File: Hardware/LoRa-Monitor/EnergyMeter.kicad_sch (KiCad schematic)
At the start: 76 parts, among them U14 ATM90E32AS-AU-R, U16 ADuM1401xRW, U17 ADuM1401xRW, U18 ADuM1401xRW, X1 16.384MHz

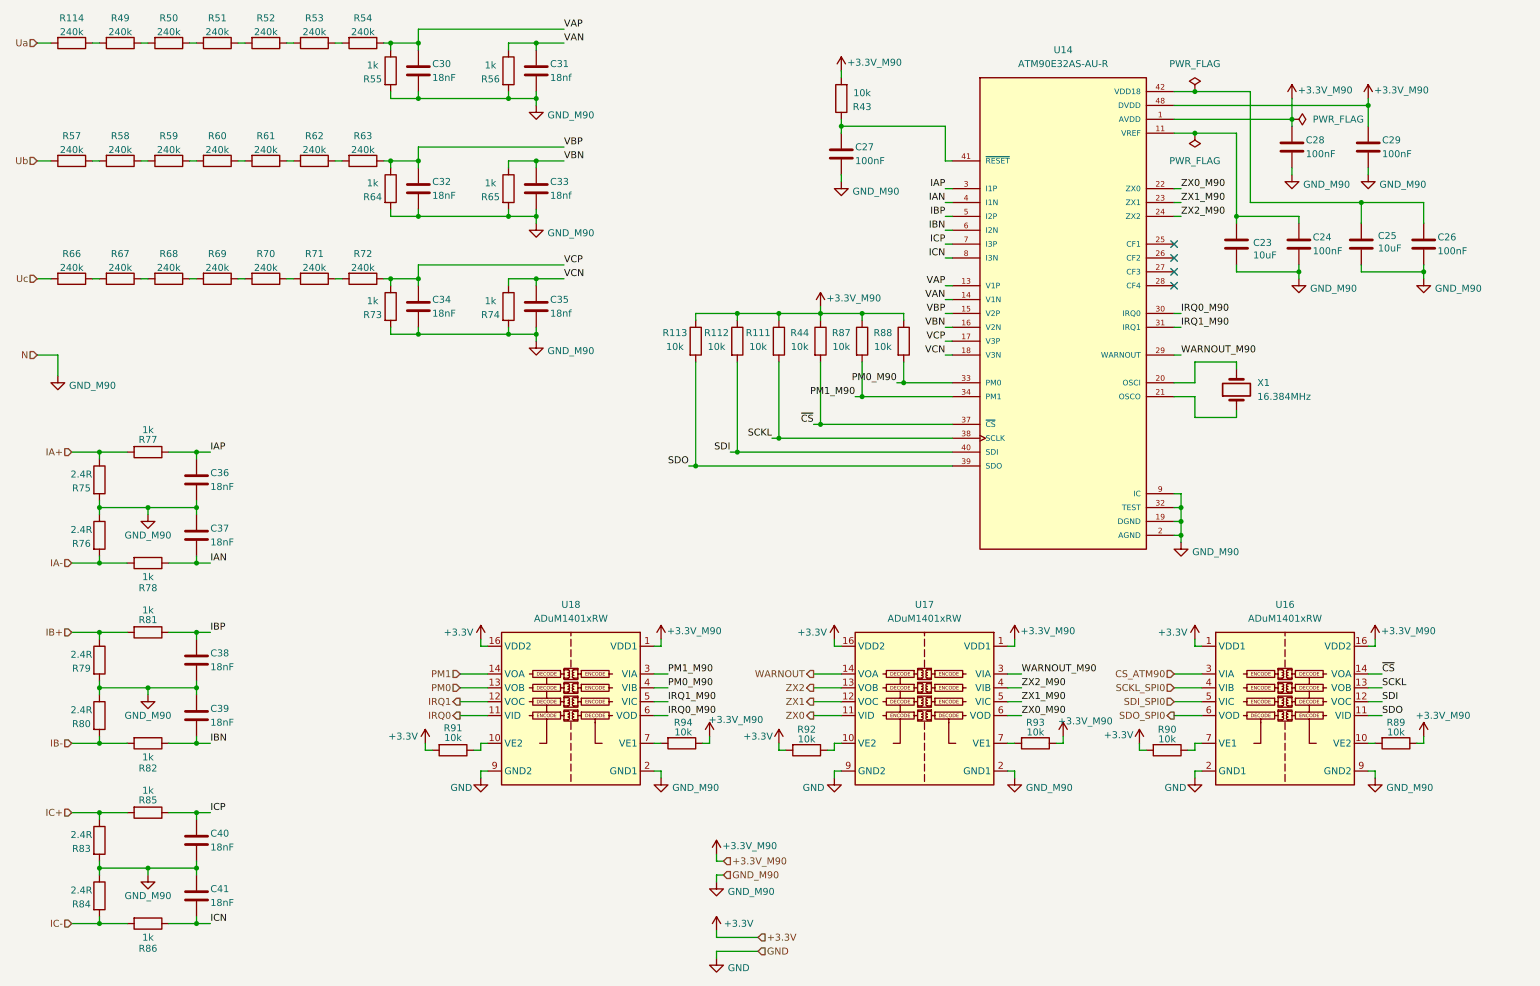
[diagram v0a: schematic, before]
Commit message: Fixed schematics and started layout
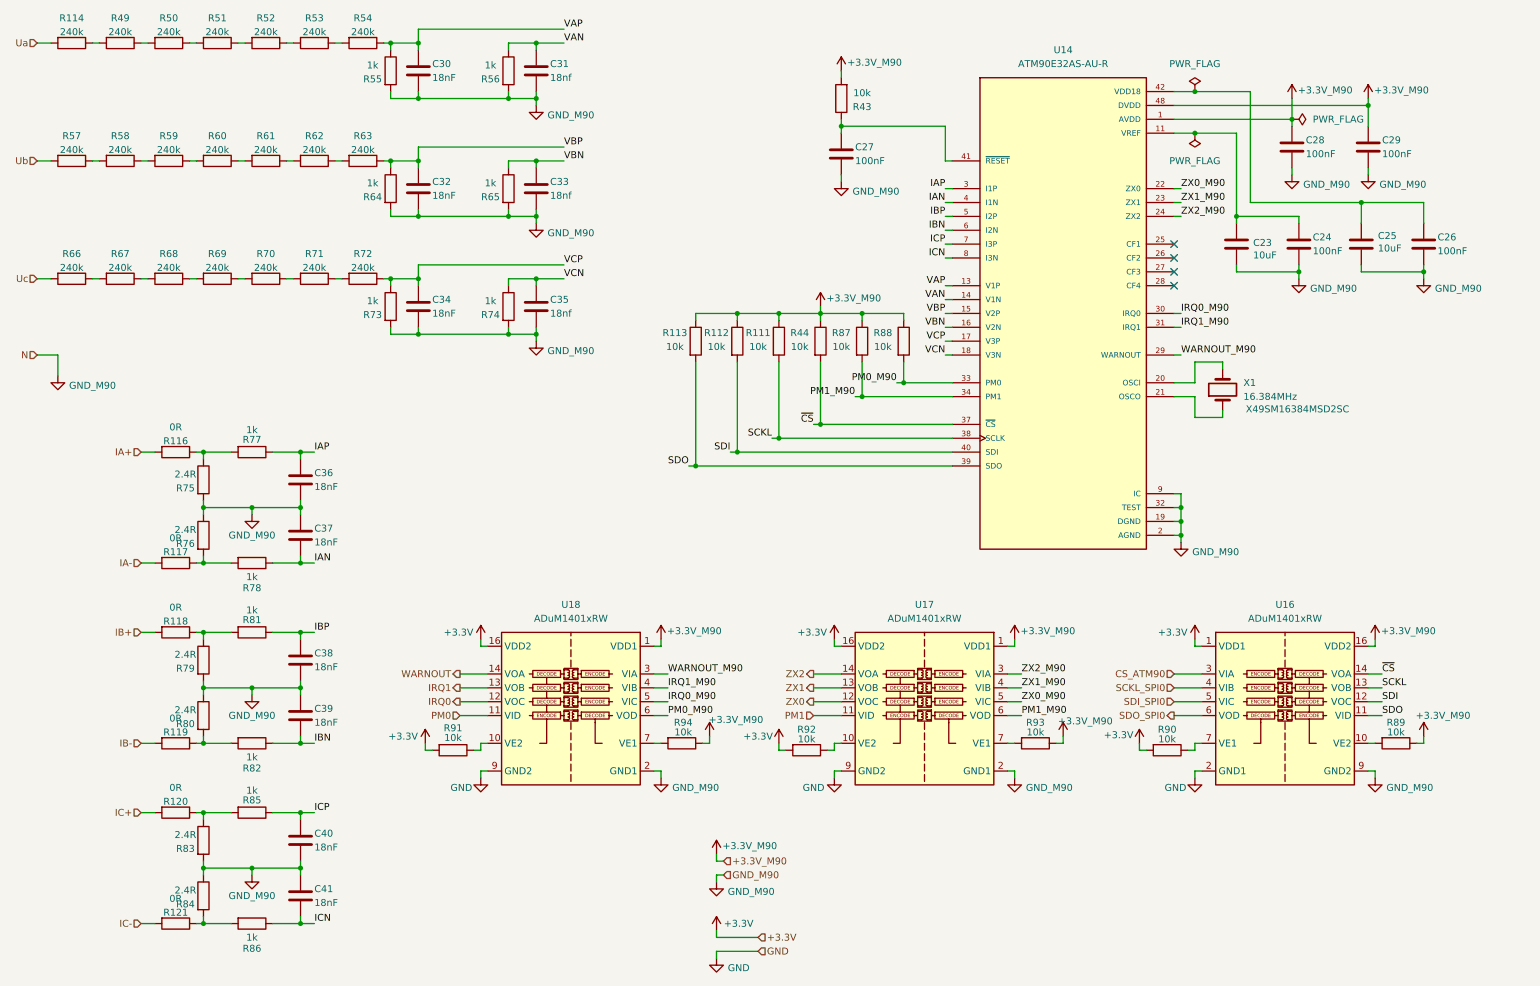
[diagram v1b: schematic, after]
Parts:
- added R116, R117, R118, R119, R120, R121: 0R, Resistor_SMD:R_0805_2012Metric, symbol Device:R
- X1: footprint (none) -> Crystal:Crystal_SMD_HC49-SD; Part # (none) -> X49SM16384MSD2SC
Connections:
- net IA+: now also R116.2; no longer R75.1, R77.2
- net IA-: now also R117.2; no longer R76.2, R78.2
- net IB+: now also R118.2; no longer R79.1, R81.2
- net IB-: now also R119.2; no longer R80.2, R82.2
- net IC+: now also R120.2; no longer R83.1, R85.2
- net IC-: now also R121.2; no longer R84.2, R86.2
- net IRQ0: now also U18.12 (VOC); no longer U18.11 (VID)
- net IRQ0_M90: now also U18.5 (VIC); no longer U18.6 (VOD)
- net IRQ1: now also U18.13 (VOB); no longer U18.12 (VOC)
- net IRQ1_M90: now also U18.4 (VIB); no longer U18.5 (VIC)
- net PM0: now also U18.11 (VID); no longer U18.13 (VOB)
- net PM0_M90: now also U18.6 (VOD); no longer U18.4 (VIB)
- net PM1: now also U17.11 (VID); no longer U18.14 (VOA)
- net PM1_M90: now also U17.6 (VOD); no longer U18.3 (VIA)
- net WARNOUT: now also U18.14 (VOA); no longer U17.14 (VOA)
- net WARNOUT_M90: now also U18.3 (VIA); no longer U17.3 (VIA)
- net ZX0: now also U17.12 (VOC); no longer U17.11 (VID)
- net ZX0_M90: now also U17.5 (VIC); no longer U17.6 (VOD)
- net ZX1: now also U17.13 (VOB); no longer U17.12 (VOC)
- net ZX1_M90: now also U17.4 (VIB); no longer U17.5 (VIC)
- net ZX2: now also U17.14 (VOA); no longer U17.13 (VOB)
- net ZX2_M90: now also U17.3 (VIA); no longer U17.4 (VIB)
- new net: R116.1, R75.1, R77.2
- new net: R117.1, R76.2, R78.2
- new net: R121.1, R84.2, R86.2
- new net: R120.1, R83.1, R85.2
- new net: R118.1, R79.1, R81.2
- new net: R119.1, R80.2, R82.2
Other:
- moved on the sheet: C36, C37, C38, C39, C40, C41, R75, R76, R77, R78, R79, R80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

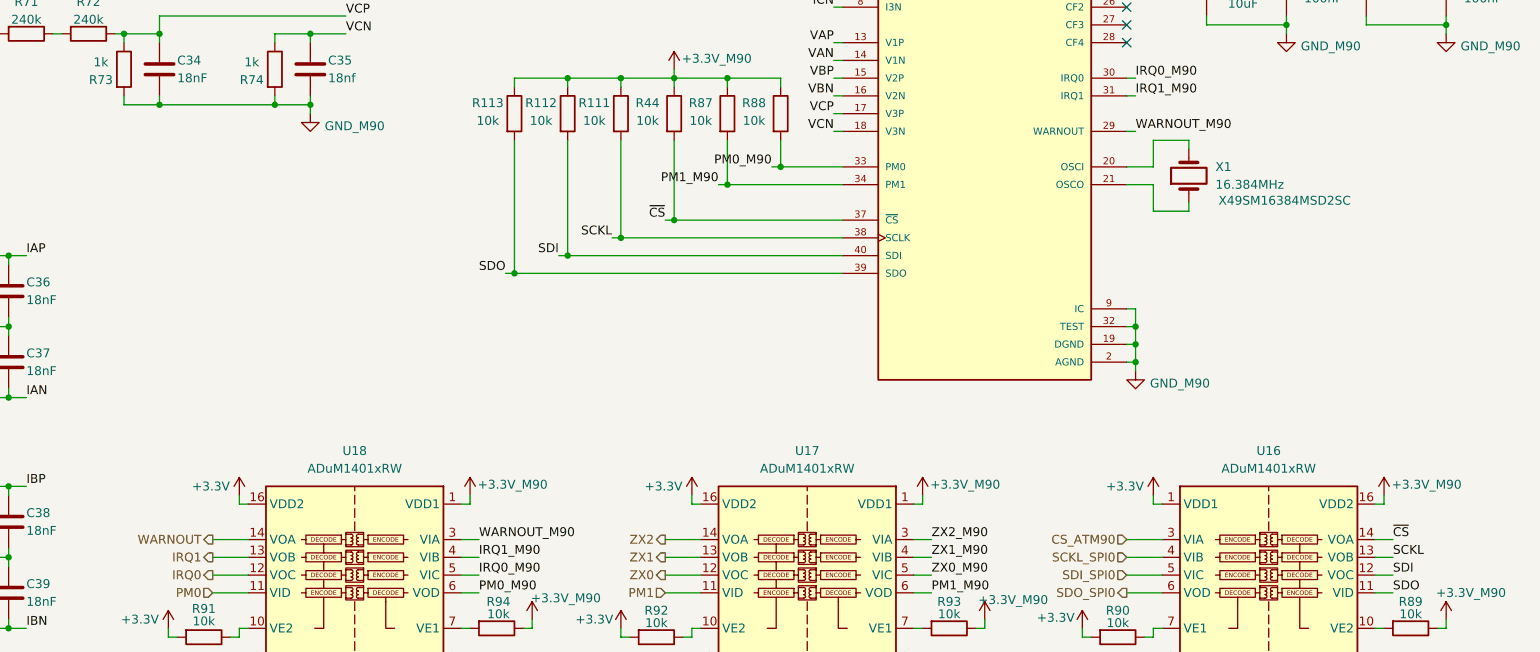
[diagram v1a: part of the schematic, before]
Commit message: Finished routing and DRC gives 0 errors.
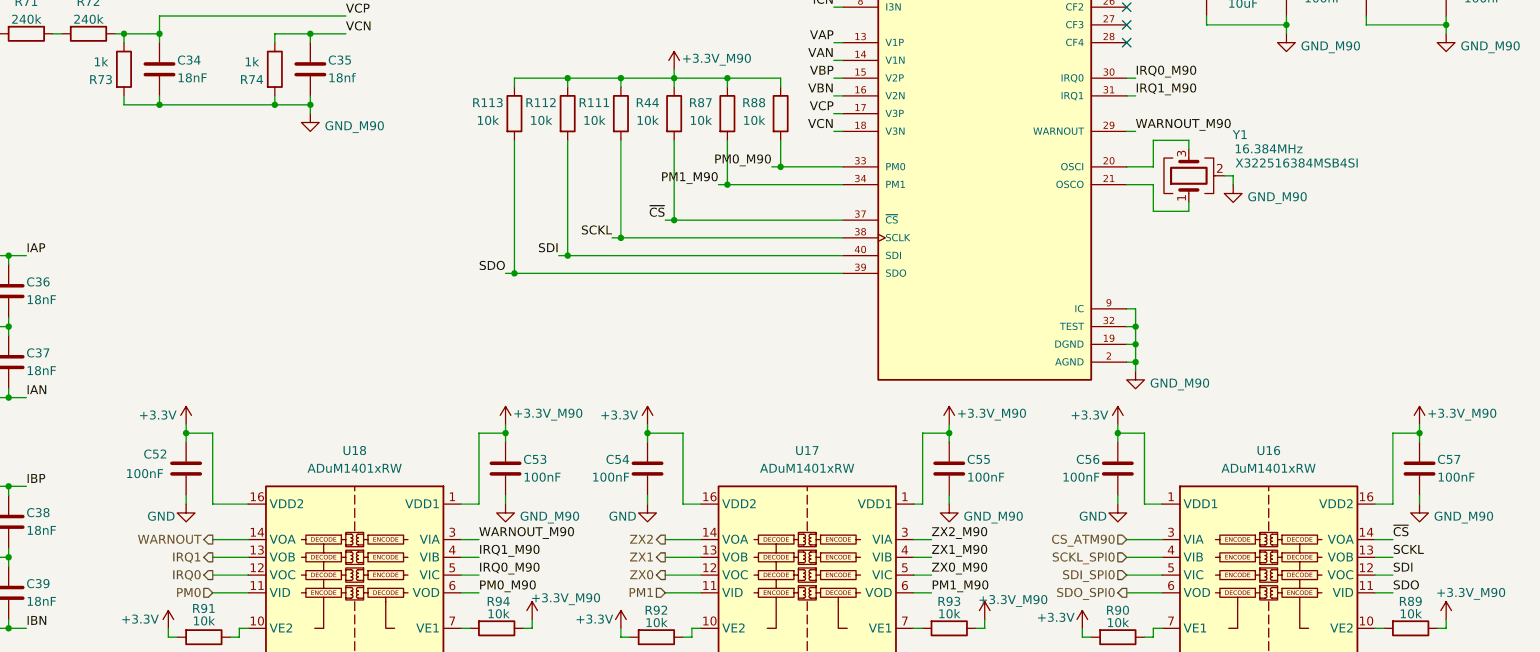
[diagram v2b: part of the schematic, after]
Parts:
- removed X1: 16.384MHz, Crystal:Crystal_SMD_HC49-SD, symbol Device:Crystal
- added C52, C53, C54, C55, C56, C57: 100nF, Capacitor_SMD:C_0805_2012Metric, symbol Device:C
- added Y1: 16.384MHz, Crystal:Crystal_SMD_3225-4Pin_3.2x2.5mm, symbol Device:Crystal_GND24
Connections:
- net +3.3V: now also C52.1, C54.1, C56.1
- net +3.3V_M90: now also C53.1, C55.1, C57.1
- net AGND: now also C53.2, C55.2, C57.2, Y1.2 (G), Y1.4 (G)
- net GND: now also C52.2, C54.2, C56.2
- net at U14.20 (OSCI): now also Y1.3
- net at U14.21 (OSCO): now also Y1.1

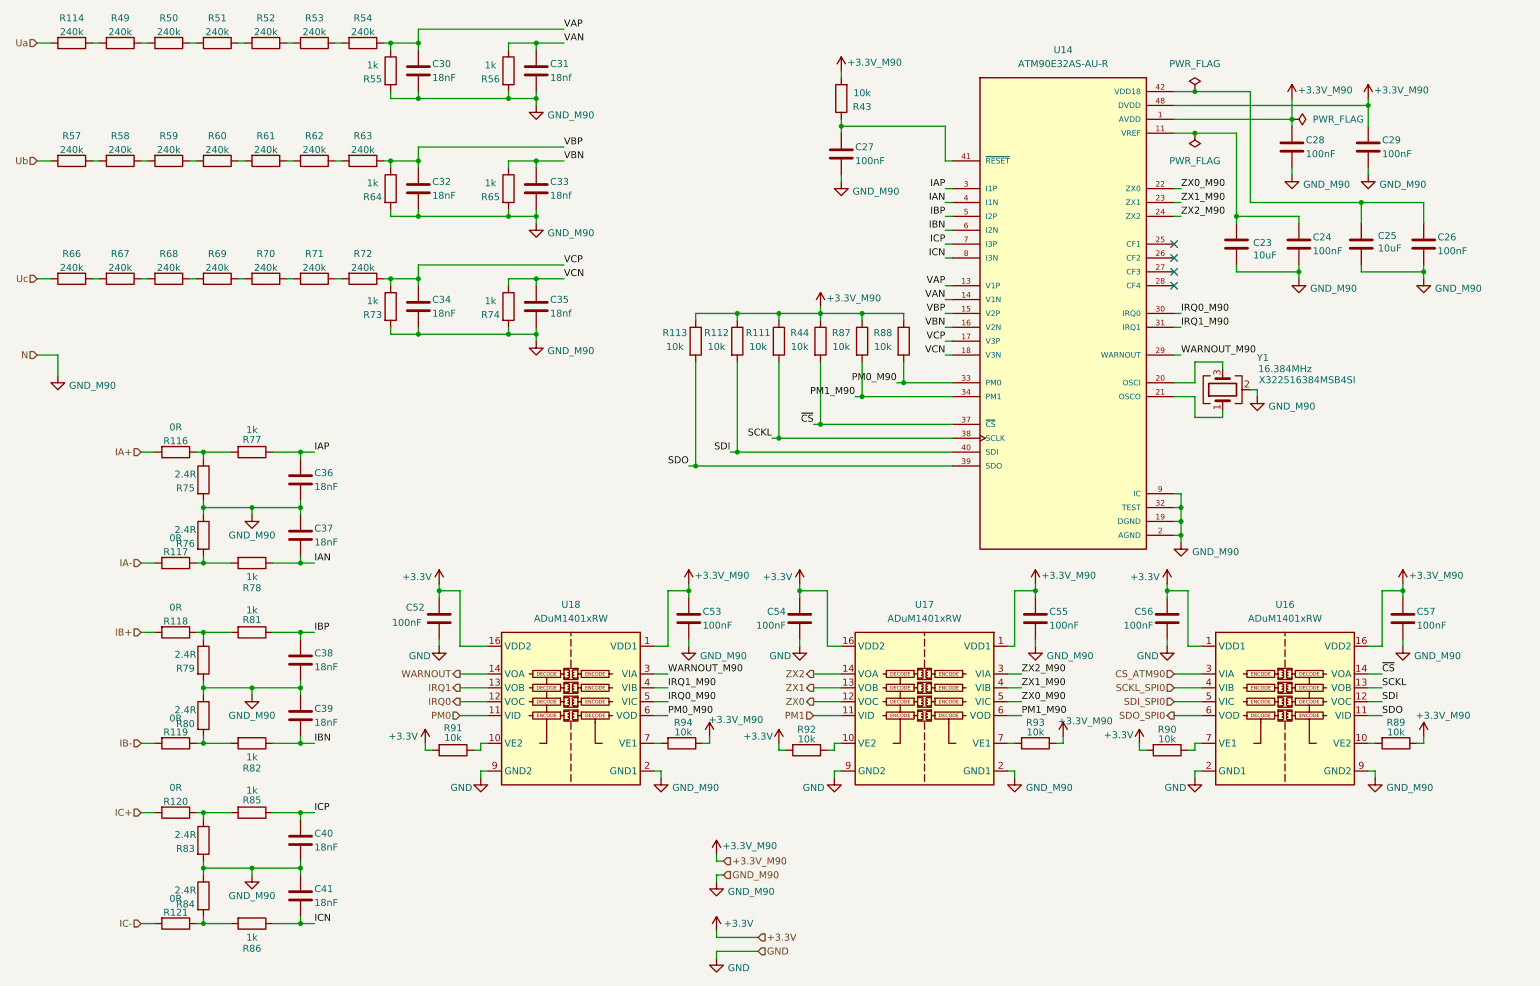
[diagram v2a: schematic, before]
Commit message: Added parameters for the productions files, changed components on LCSC to reduce the price of BoM, minimal changes on the routing.
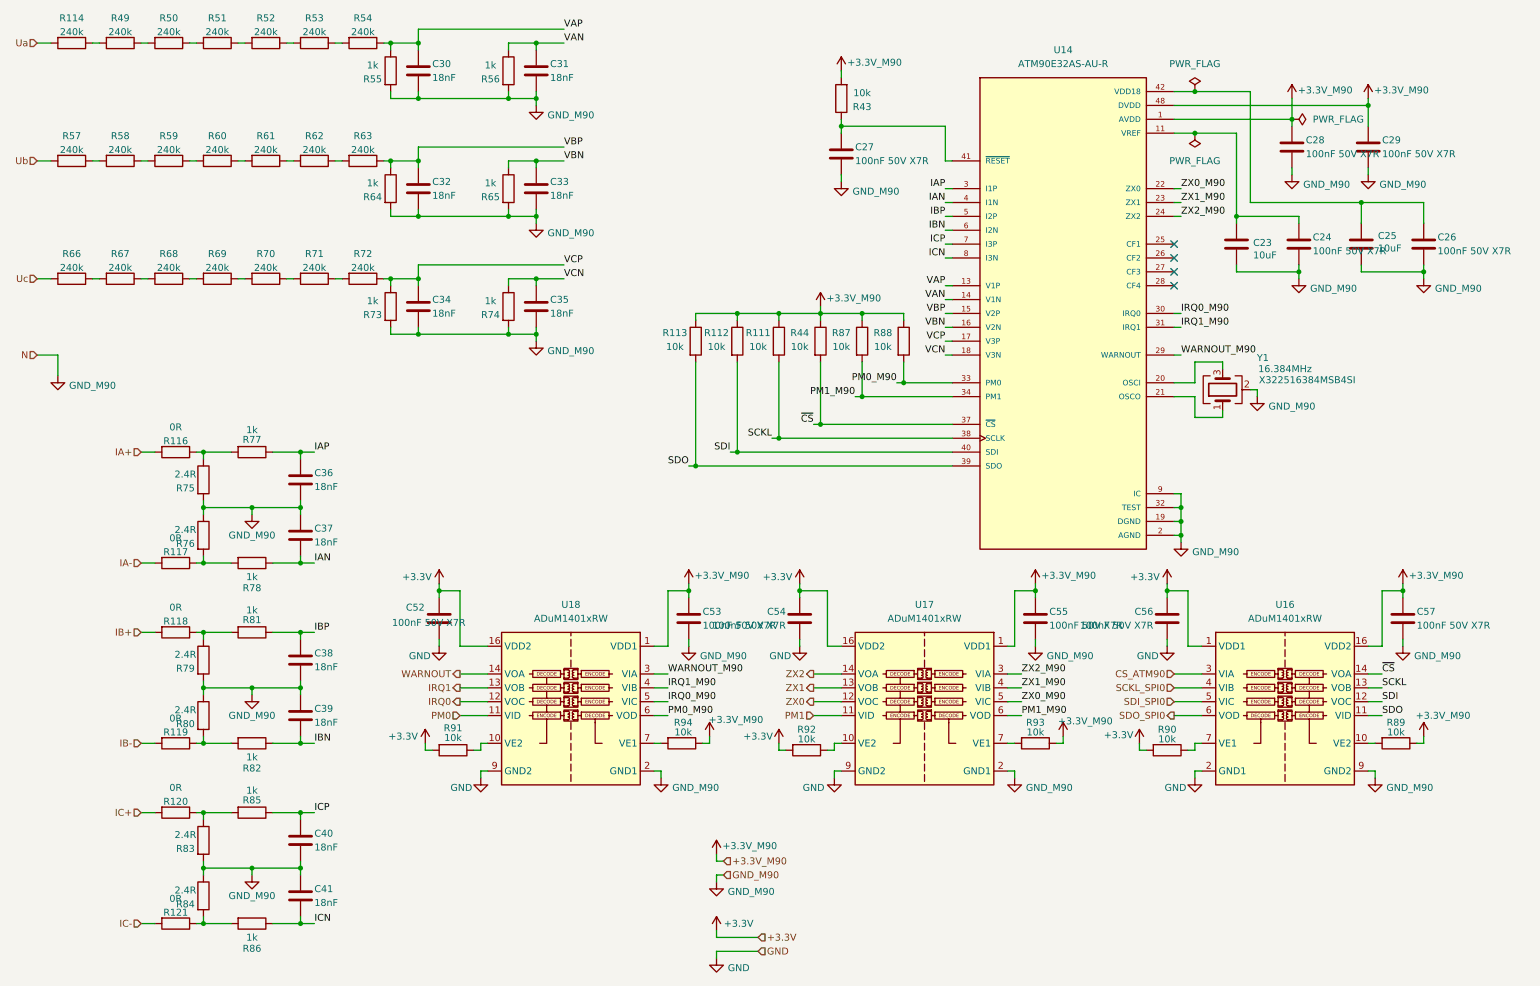
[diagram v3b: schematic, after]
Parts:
- C23, C25: LCSC Part # (none) -> C15850
- C24, C26, C27, C28, C29, C52, C53, C54, C55, C56, C57: value 100nF -> 100nF 50V X7R; LCSC Part # (none) -> C49678
- C30, C32, C34, C36, C37, C38, C39, C40, C41: LCSC Part # (none) -> C1723
- C31, C33, C35: value 18nf -> 18nF; LCSC Part # (none) -> C1723
- R111, R112, R113, R43, R44, R87, R88, R89, R90, R91, R92, R93, R94: LCSC Part # (none) -> C17414
- R114, R49, R50, R51, R52, R53, R54, R57, R58, R59, R60, R61, R62, R63, R66, R67, R68, R69, R70, R71, R72: LCSC Part # (none) -> C18001
- R116, R117, R118, R119, R120, R121: LCSC Part # (none) -> C17477
- R55, R56, R64, R65, R73, R74, R77, R78, R81, R82, R85, R86: LCSC Part # (none) -> C17513
- R75, R76, R79, R80, R83, R84: LCSC Part # (none) -> C17528
- U14: FT Rotation Offset (none) -> -90; LCSC Part # (none) -> C177153
- U16, U17, U18: FT Rotation Offset (none) -> 90; LCSC Part # (none) -> C91762
- Y1: LCSC Part # (none) -> C13739
